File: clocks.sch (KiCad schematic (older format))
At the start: 14 parts, among them J2 UPDI TTL, U11 ATtiny1614-SS, U13 AS1115-BSST, U14 ACDA02-41SGWA-F01, U2 TPS7A0533PDBVR

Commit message: fixed pins
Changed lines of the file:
@@
 NoConn ~ 8150 2900
 NoConn ~ 8150 3000
+Connection ~ 7550 800
 $EndSCHEMATC

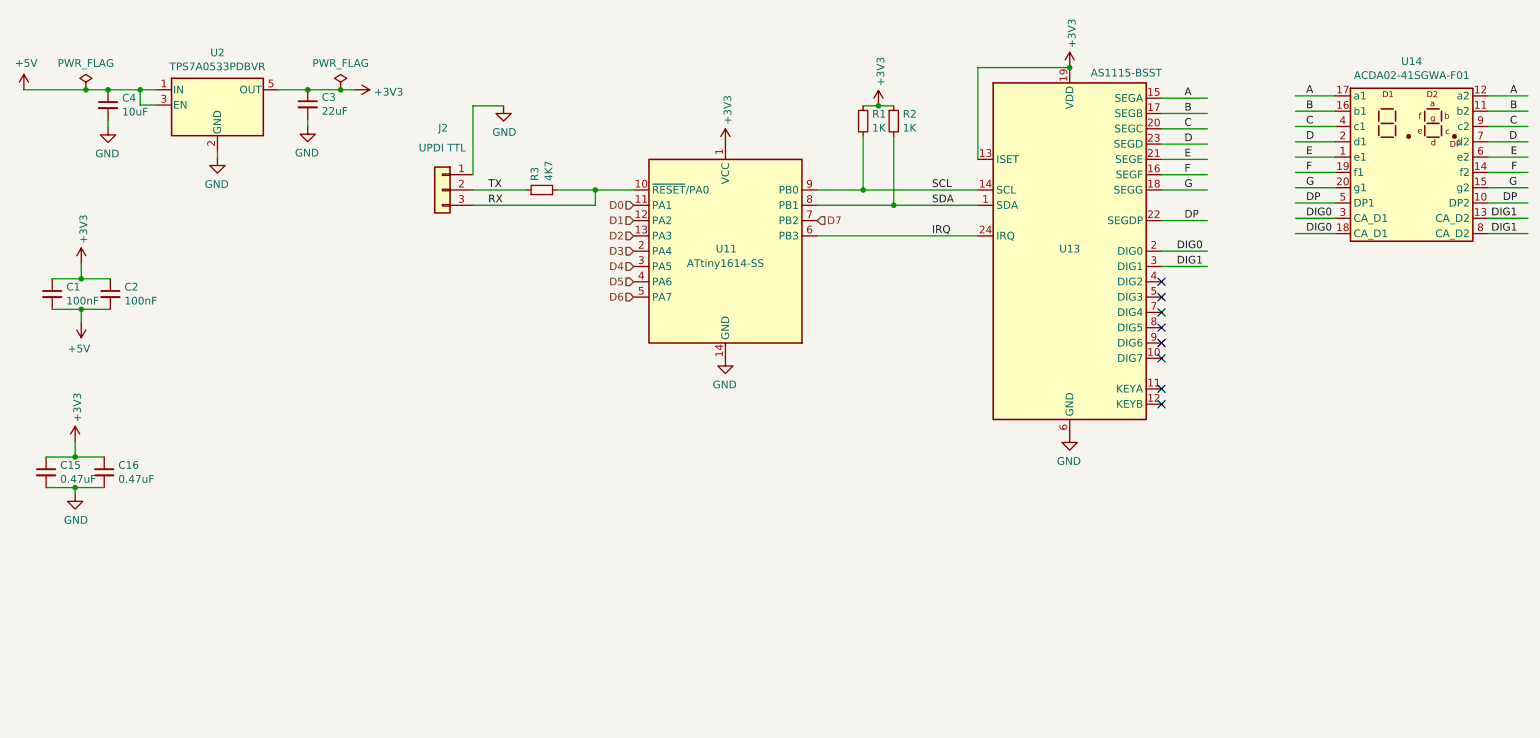
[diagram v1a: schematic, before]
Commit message: changed part layout, removed switch
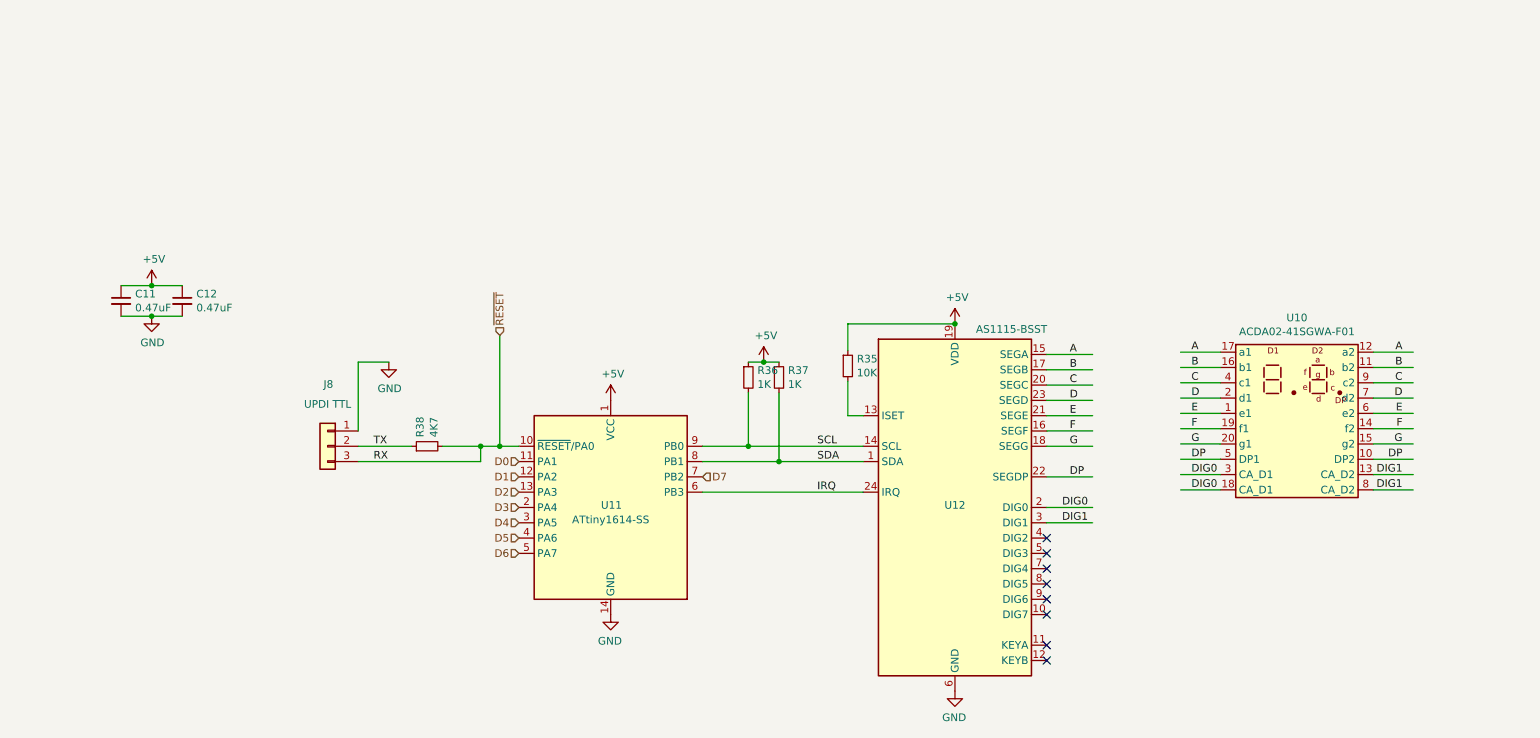
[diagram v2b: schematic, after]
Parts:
- removed C1, C2: 100nF, Capacitor_SMD:C_0805_2012Metric_Pad1.15x1.40mm_HandSolder, symbol sbc_z80-rescue:C_Small-Device
- removed C3: 22uF, Capacitor_SMD:C_0805_2012Metric_Pad1.15x1.40mm_HandSolder, symbol sbc_z80-rescue:C_Small-Device
- removed C4: 10uF, Capacitor_SMD:C_0805_2012Metric_Pad1.15x1.40mm_HandSolder, symbol sbc_z80-rescue:C_Small-Device
- removed U2: TPS7A0533PDBVR, Package_TO_SOT_SMD:SOT-23-5, symbol sbc_z80-rescue:TPS7A0533PDBVR-Regulator_Linear
- added R35: 10K, Resistor_SMD:R_0603_1608Metric_Pad1.05x0.95mm_HandSolder, symbol sbc_z80-rescue:R_Small-Device
- renumbered C15 to C11, C16 to C12, J2 to J8, R1 to R36, R2 to R37, R3 to R38, U14 to U10, U13 to U12
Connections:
- net labels added: ~RESET
- net labels removed: +3V3
- wire segments 74 -> 56
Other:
- moved on the sheet: C11, C12, J8, R36, R37, R38, U10, U11, U12
